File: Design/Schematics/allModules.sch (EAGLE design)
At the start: 209 parts, among them IC1 MAX7219CNG, IC2 MAX7219CNG, IC3 MAX7219CNG, IC4 MAX7219CNG, IC5 MCP3008, IC6 MCP23017SP, U1 328P, U2 328P, U3 328P, U4 328P, U5 328P, U6 328P

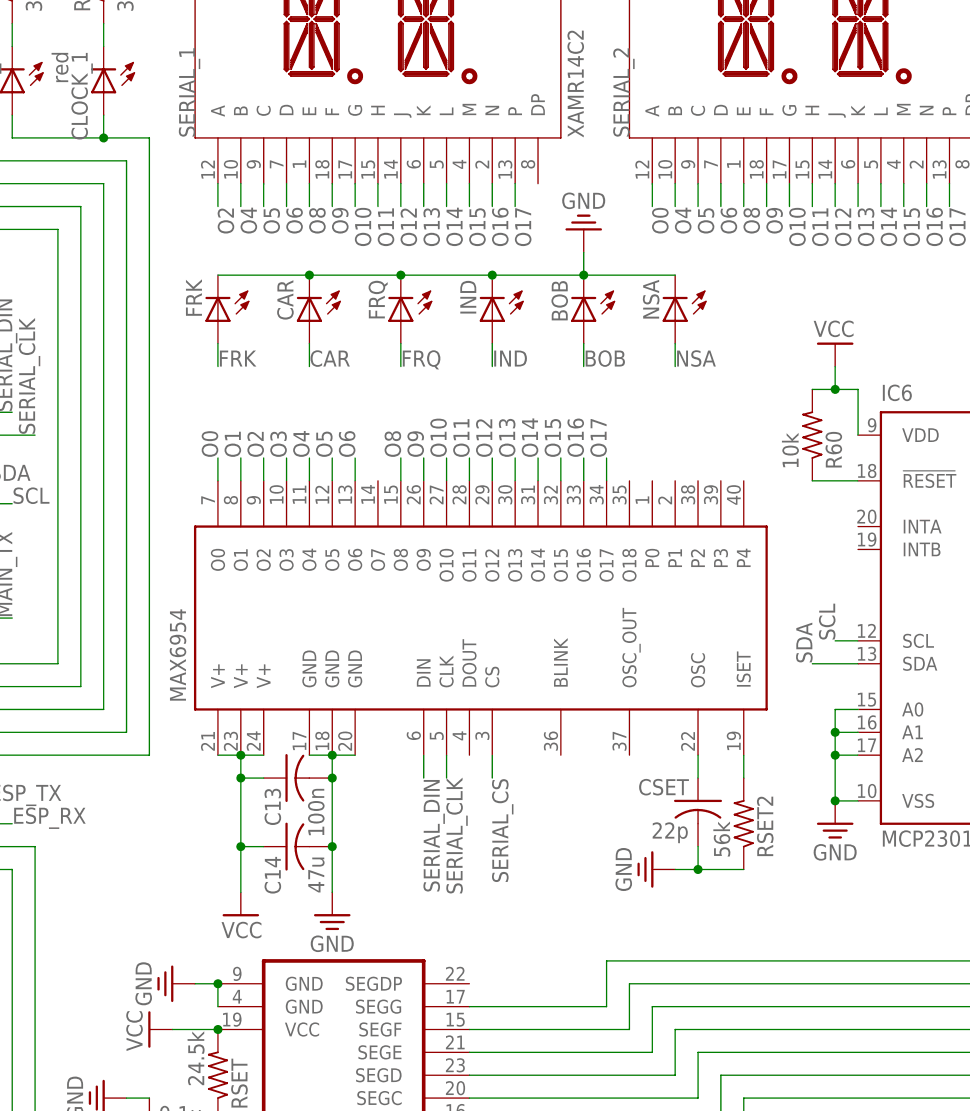
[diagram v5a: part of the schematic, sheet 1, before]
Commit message: Added resistors to indicator led's
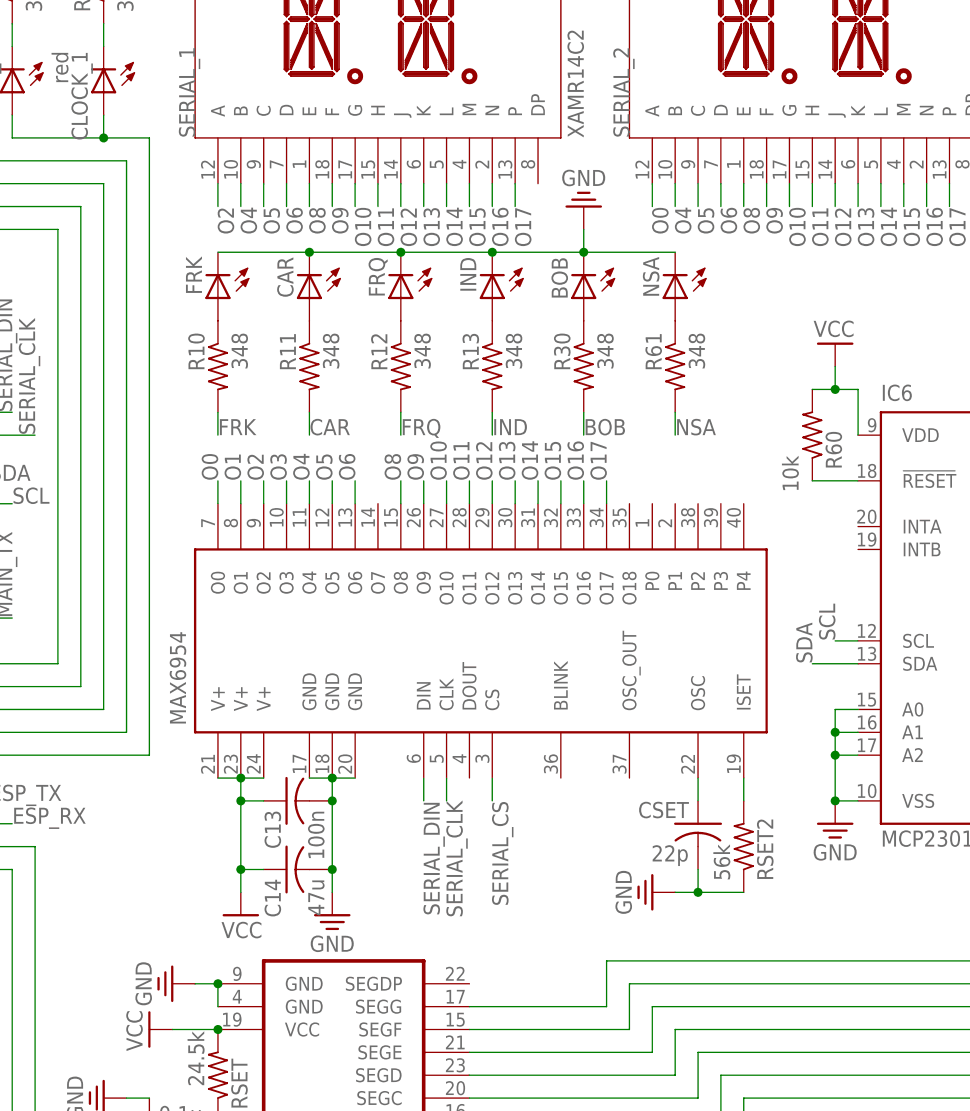
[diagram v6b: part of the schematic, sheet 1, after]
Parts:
- added R10, R11, R12, R13, R30, R61: 348, BeagleBone_Black_Wireless:R-US_0204/7
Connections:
- new net N$127: FRK.A, R10.1
- new net N$143: CAR.A, R11.1
- new net N$146: FRQ.A, R12.1
- new net N$147: IND.A, R13.1
- new net N$148: BOB.A, R30.1
- new net N$151: NSA.A, R61.1
- net BOB: now also R30.2; no longer BOB.A
- net CAR: now also R11.2; no longer CAR.A
- net FRK: now also R10.2; no longer FRK.A
- net FRQ: now also R12.2; no longer FRQ.A
- net IND: now also R13.2; no longer IND.A
- net NSA: now also R61.2; no longer NSA.A
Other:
- moved on the sheet: BOB, C13, C14, CAR, CSET, FRK, FRQ, IND, MAX6954, NSA, RSET2
